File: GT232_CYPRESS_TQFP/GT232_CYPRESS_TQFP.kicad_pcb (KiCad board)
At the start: 2 copper layers, 50.7 x 13.8 mm, 35 parts, among them IC1 CY8C4014LQI-421, IC2 CY8C4014LQI-422, IC3 CY8C4024LQI-S401, J1 Conn_01x05, U1 LMR51610XDBVR

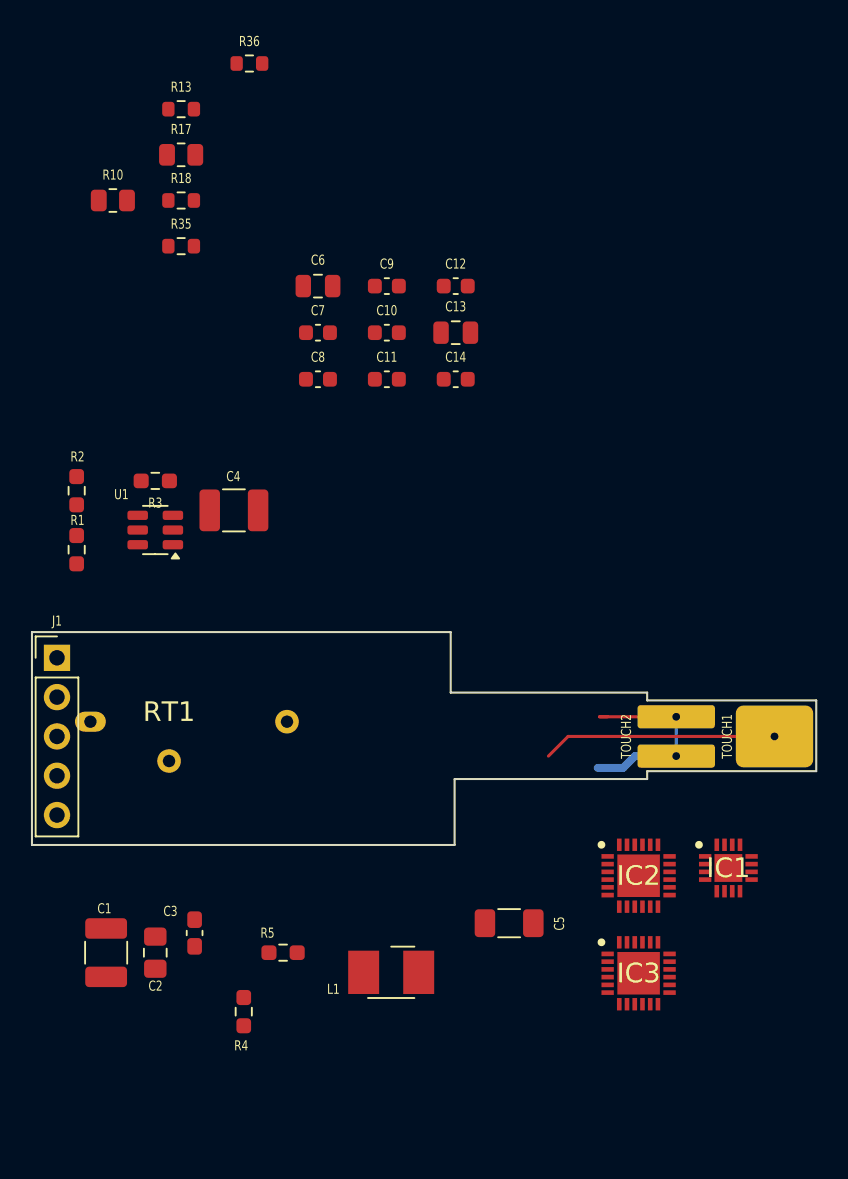
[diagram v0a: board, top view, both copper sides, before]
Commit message: Aggiornato schema e PCB del modello con micro 4014
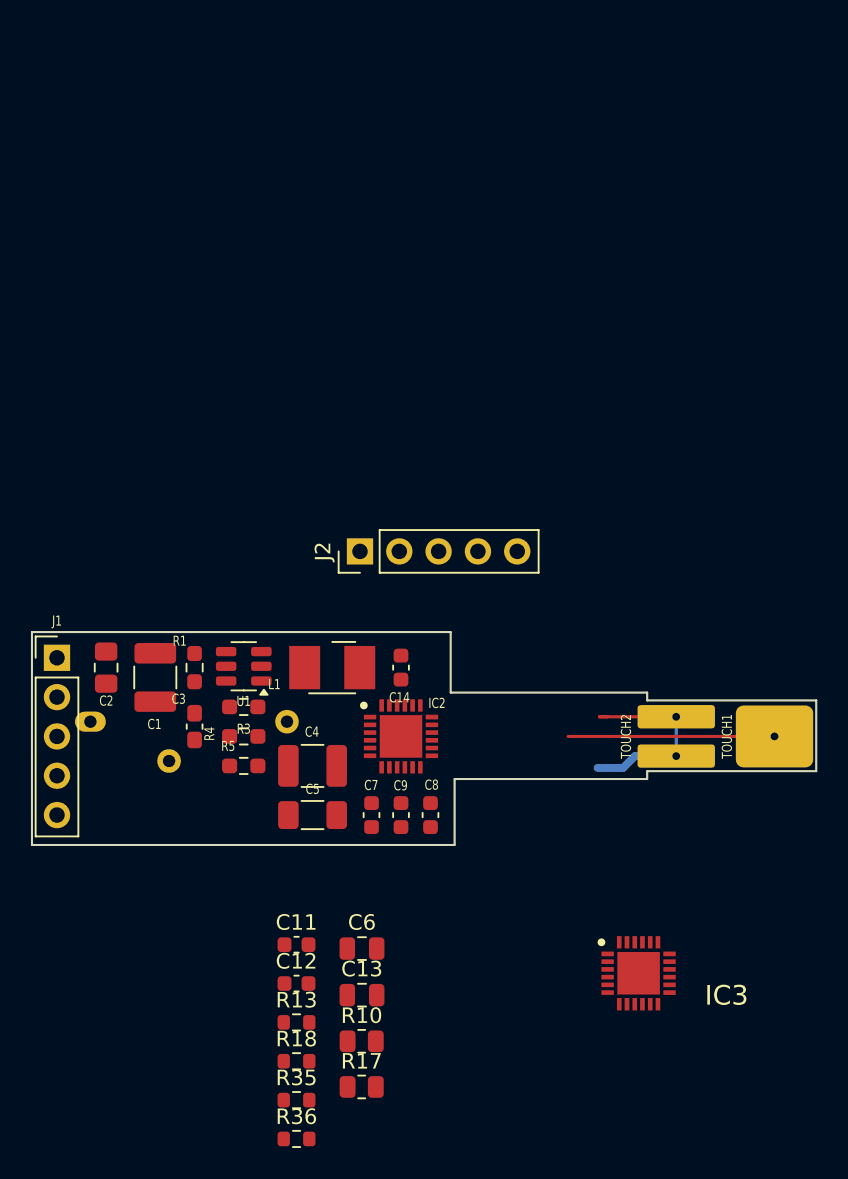
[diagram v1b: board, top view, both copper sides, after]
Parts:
- removed C10: 1uF 10V, Capacitor_SMD:C_0603_1608Metric
- removed IC1: CY8C4014LQI-421, MyPCB:QFN50P300X300X60-17N-D
- removed R2: 10K, Resistor_SMD:R_0603_1608Metric_Pad0.98x0.95mm_HandSolder
- added J2: Conn_01x05, Connector_PinHeader_2.54mm:PinHeader_1x05_P2.54mm_Vertical, F.Cu at (144.4, 92.9)
- moved R36 69.5 mm to (140.3, 130.9)
- moved R17 61.3 mm to (144.5, 127.5)
- moved R13 59.5 mm to (140.3, 123.3)
- moved R10 56.6 mm to (144.5, 124.6)
- moved R18 56.1 mm to (140.3, 125.9)
- moved R35 55.7 mm to (140.3, 128.4)
- moved C12 46.2 mm to (140.3, 120.8)
- moved C13 43.2 mm to (144.5, 121.6)
- moved C6 42.9 mm to (144.5, 118.6)
- moved C11 37.0 mm to (140.3, 118.3)
- moved C9 34.2 mm to (147.0, 109.9), turned to -90 degrees
- moved C7 31.4 mm to (145.1, 109.9), turned to -90 degrees
- moved C8 29.1 mm to (148.9, 109.9), turned to -90 degrees
- moved L1 20.1 mm to (142.6, 100.4)
- moved C14 19.0 mm to (147.0, 100.4), turned to 90 degrees
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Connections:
- C11 pad 1: 3V3 -> unconnected-(C11-Pad1)
- C11 pad 2: GND -> unconnected-(C11-Pad2)
- C12 pad 1: 3V3 -> unconnected-(C12-Pad1)
- C12 pad 2: GND -> unconnected-(C12-Pad2)
- C14 pad 1: 3V3 -> XRES
- C14 pad 2: XRES -> GND
- C6 pad 1: GND -> Net-(C6-Pad1)
- C7 pad 1: GND -> 5V
- C7 pad 2: Net-(C7-Pad2) -> GND
- C8 pad 1: GND -> 5V
- C8 pad 2: Net-(C7-Pad2) -> GND
- C9 pad 1: 3V3 -> 5V
- IC2 pad 21: unconnected-(IC2-P3.0-Pad21) -> SW_D
- IC2 pad 22: unconnected-(IC2-P3.1-Pad22) -> SW_C
- IC2 pad 24: unconnected-(IC2-XRES-Pad24) -> XRES
- IC2 pad 25: unconnected-(IC2-EP-Pad25) -> GND
- IC2 pad 6: unconnected-(IC2-VCCD-Pad6) -> 5V
- IC2 pad 7: unconnected-(IC2-VDD-Pad7) -> 5V
- IC2 pad 8: unconnected-(IC2-VSS-Pad8) -> GND
- J1 pad 1: TX -> 12V
- J1 pad 2: SW_D -> unconnected-(J1-Pin_2-Pad2)
- J1 pad 3: SW_C -> GND
- J1 pad 4: 12V -> unconnected-(J1-Pin_4-Pad4)
- J1 pad 5: GND -> unconnected-(J1-Pin_5-Pad5)
- R10 pad 1: GND -> Net-(C6-Pad1)
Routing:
- net /TOUCH1: track 15.1 -> 13.3 mm
